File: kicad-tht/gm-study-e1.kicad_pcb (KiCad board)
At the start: 2 copper layers, 100 x 70 mm, 99 parts, among them J1 Conn_01x16, SW0 SW_SPDT, SW1 SW_SPDT, SW2 SW_SPDT, SW3 SW_SPDT, SW4 SW_SPDT, SW5 SW_SPDT, SW6 SW_SPDT, SW7 SW_SPDT, SW8 SW_SPDT, SW9 SW_SPDT, U1 SGM6603-5.0, U2 LSF0204, U3 LSF0204, U4 LSF0204

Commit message: file updates
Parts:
- removed JP1: Jumper, Connector_PinHeader_2.54mm:PinHeader_1x02_P2.54mm_Vertical
- R1, R10, R2, R3, R4, R5, R6, R7, R8, R9: value 10K -> 100K
- R11, R12, R13, R14, R15, R16, R17, R18, R19, R20: value 160 -> 200
- R30: value 160 -> 100
- RA1, RA10, RA11, RA12, RA2, RA3, RA4, RA5, RA6, RA7, RA8, RA9: value 180 -> 200
- moved BZ1 2.05 mm to (106.0, 73.0)
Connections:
- SW0 pad 3: Net-(JP1-Pad1) -> VIO_2V5
- SW1 pad 3: Net-(JP1-Pad1) -> VIO_2V5
- SW2 pad 3: Net-(JP1-Pad1) -> VIO_2V5
- SW3 pad 3: Net-(JP1-Pad1) -> VIO_2V5
- SW4 pad 3: Net-(JP1-Pad1) -> VIO_2V5
- SW5 pad 3: Net-(JP1-Pad1) -> VIO_2V5
- SW6 pad 3: Net-(JP1-Pad1) -> VIO_2V5
- SW7 pad 3: Net-(JP1-Pad1) -> VIO_2V5
- SW8 pad 3: Net-(JP1-Pad1) -> VIO_2V5
- SW9 pad 3: Net-(JP1-Pad1) -> VIO_2V5
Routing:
- net Net-(JP1-Pad1): track 64.2 -> 0.00 mm
- net VIO_2V5: track 180.7 -> 219.2 mm
- net IO_SA_A0: track 41.6 -> 39.6 mm
- net Net-(C6-Pad1): track 17.1 -> 17.6 mm
- net Net-(C4-Pad1): track 17.0 -> 17.5 mm
- net Net-(C3-Pad1): track 17.0 -> 17.5 mm
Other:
- board text removed: "SW0..9 pull-up"

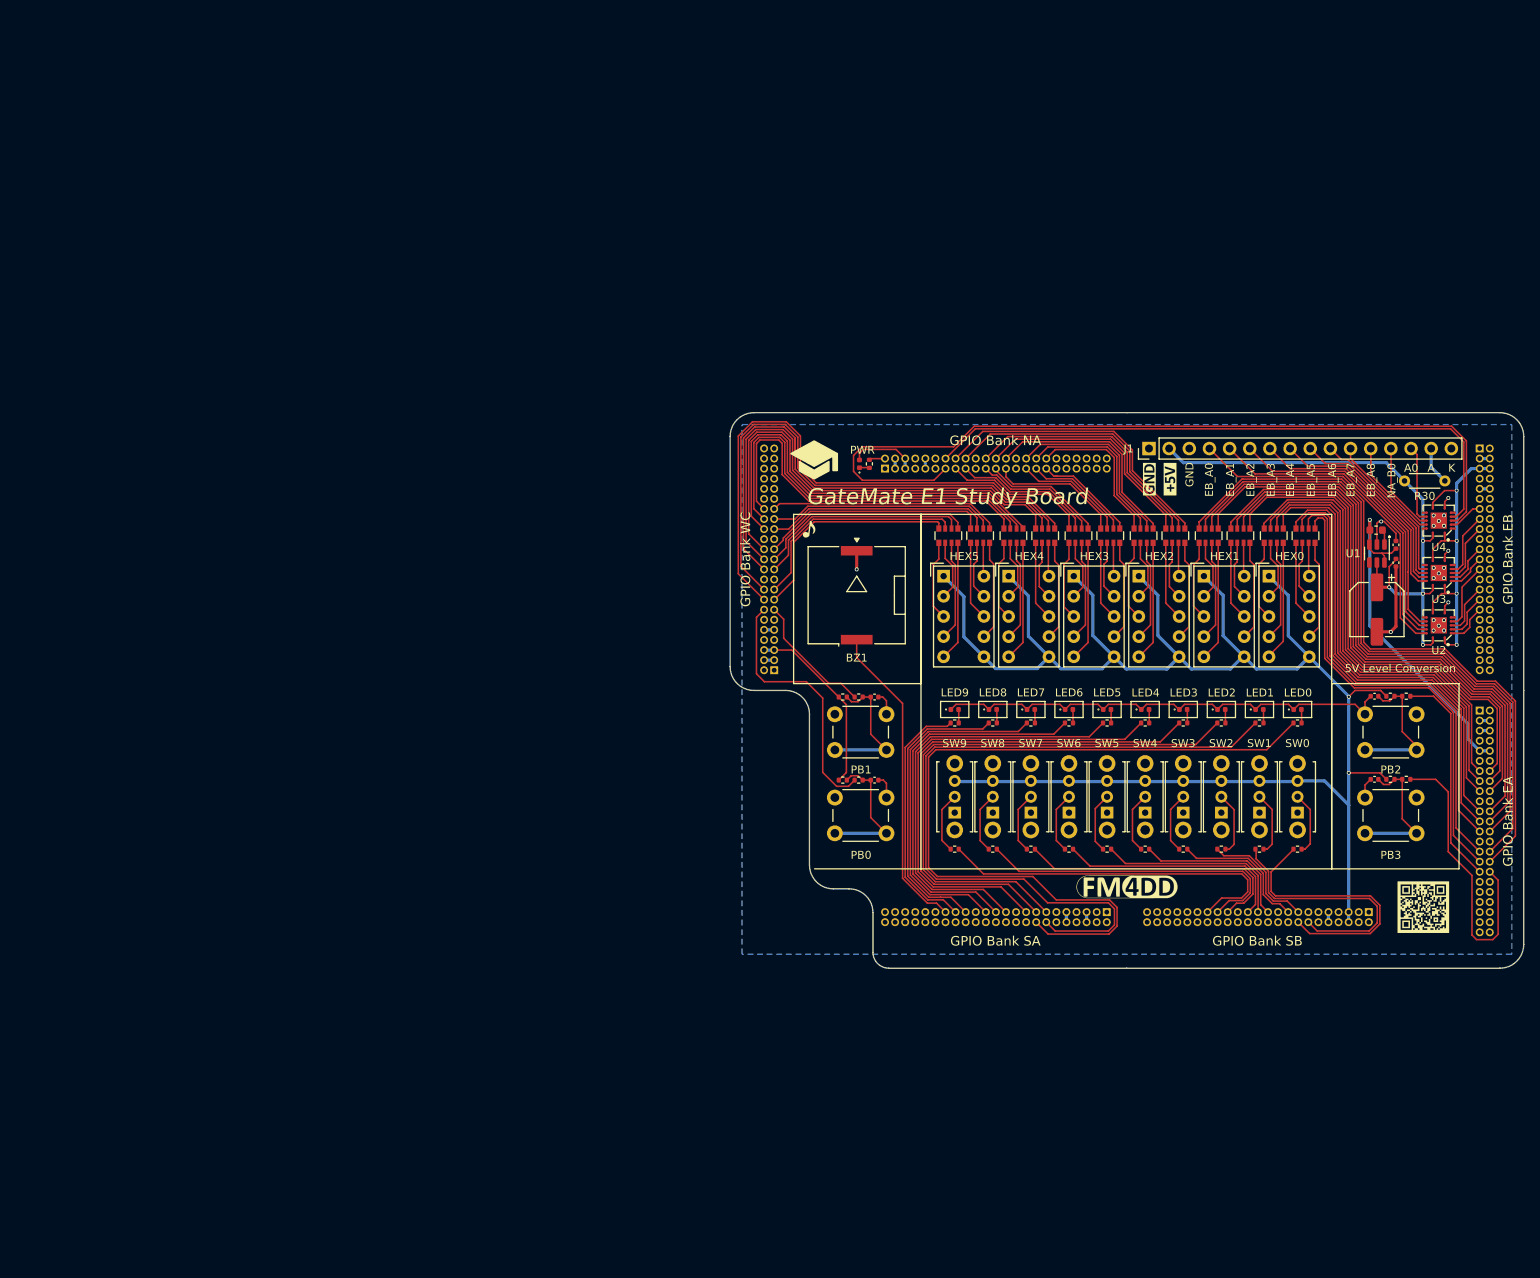
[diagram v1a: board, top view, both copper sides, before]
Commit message: New THT PCB v1.1 updates J1 level translation IC
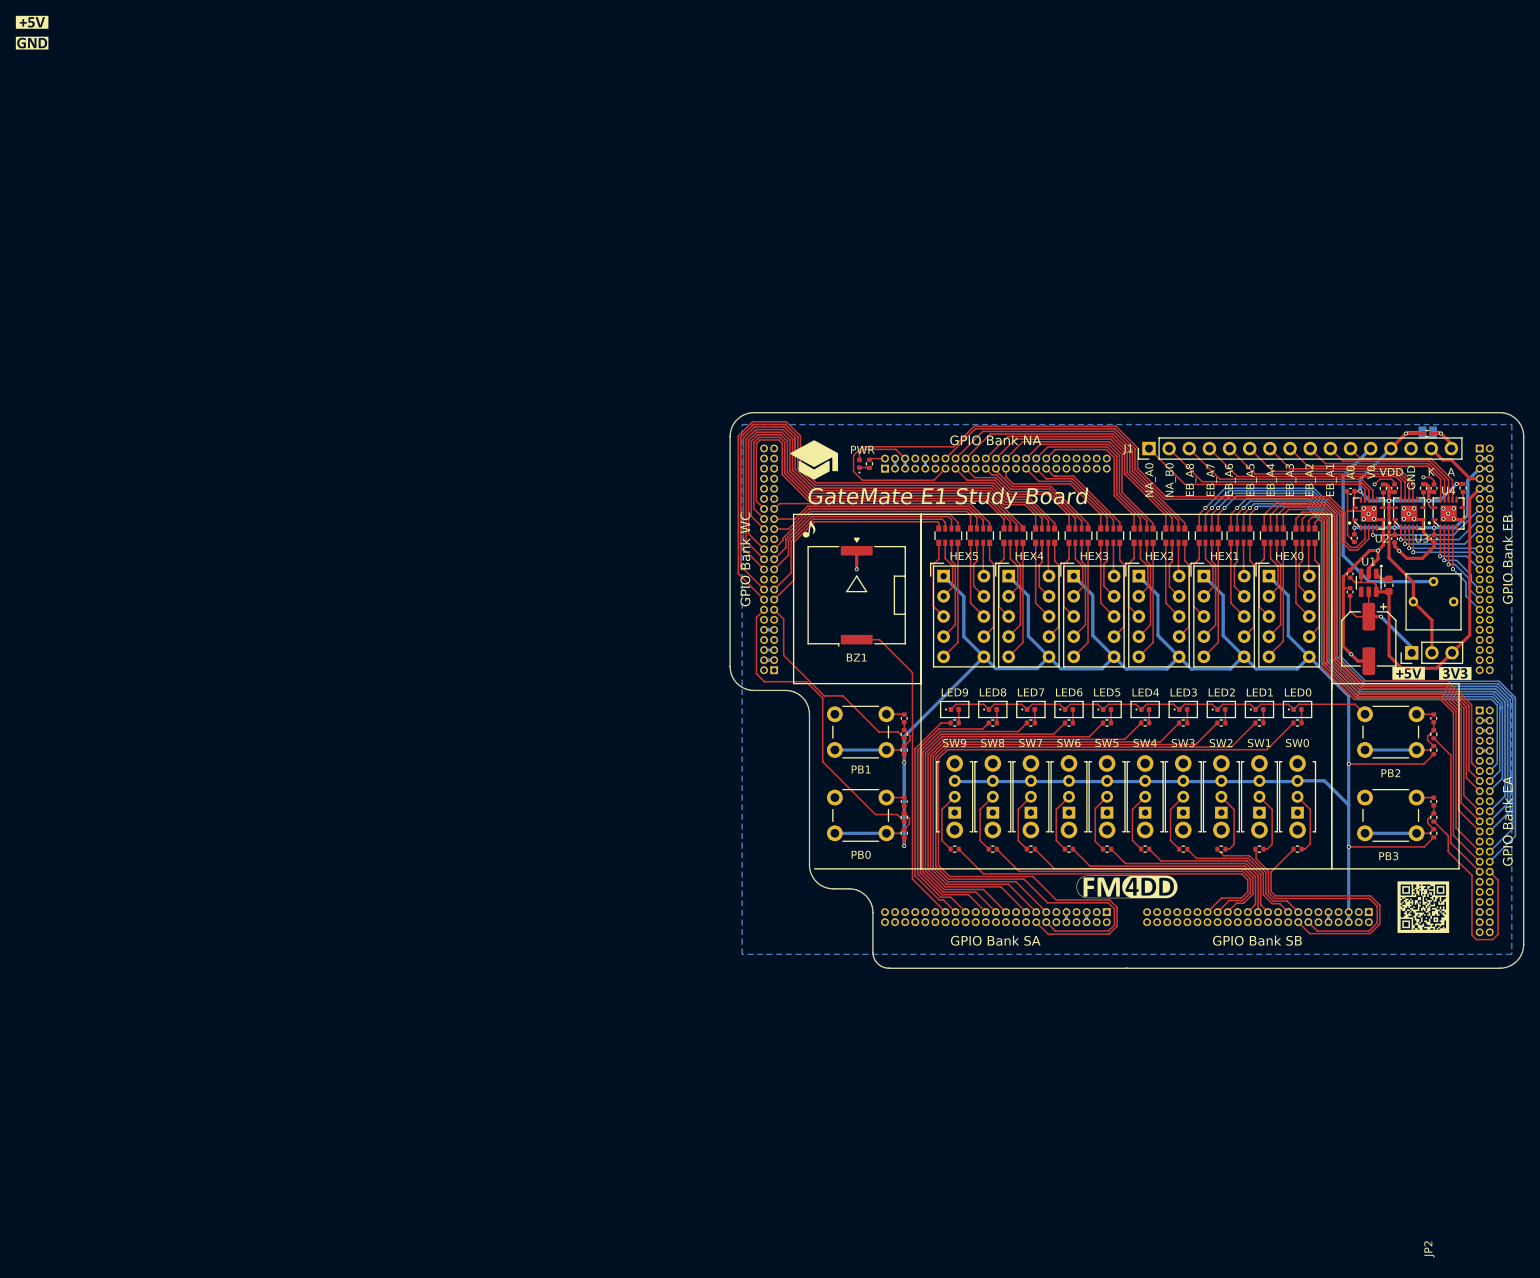
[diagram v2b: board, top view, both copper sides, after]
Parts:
- added C10: 0.1uF, Capacitor_SMD:C_0402_1005Metric, F.Cu at (178.7, 65.9)
- added C11: 0.1uF, Capacitor_SMD:C_0402_1005Metric, F.Cu at (173.7, 59.5)
- added C12: 0.1uF, Capacitor_SMD:C_0402_1005Metric, F.Cu at (168.2, 59.9)
- added C13: 0.1uF, Capacitor_SMD:C_0402_1005Metric, F.Cu at (178.7, 59.5)
- added C8: 0.1uF, Capacitor_SMD:C_0402_1005Metric, F.Cu at (168.7, 65.8)
- added C9: 0.1uF, Capacitor_SMD:C_0402_1005Metric, F.Cu at (173.7, 65.9)
- added JP1: SolderJumper_2_Open, Jumper:SolderJumper-2_P1.3mm_Open_Pad1.0x1.5mm, B.Cu at (177.9, 52.5)
- added JP2: UP_PWR, Connector_PinHeader_2.54mm:PinHeader_1x03_P2.54mm_Vertical, F.Cu at (175.9, 80.3)
- added LB5: Label_3V3, FM4DD:Label_3V3, F.Cu at (181.4, 82.9)
- added LB6: Label_5V, FM4DD:Label_5V, F.Cu at (175.5, 82.8)
- added R31: 10K, Resistor_SMD:R_0402_1005Metric, F.Cu at (172.3, 59.5)
- added R32: 10K, Resistor_SMD:R_0402_1005Metric, F.Cu at (177.4, 59.5)
- added R33: 10K, Resistor_SMD:R_0402_1005Metric, F.Cu at (182.4, 59.5)
- added RV1: 10K, FM4DD:Potentiometer_Bourns_3362P_Vertical, F.Cu at (178.6, 73.5)
- J1: value Conn_01x16 -> CharLCD_Header; footprint Connector_PinHeader_2.54mm:PinHeader_1x16_P2.54mm_Vertical -> FM4DD:CharLCD Header
- LED10: footprint FM4DD:LED_0402_FPGA -> FM4DD:LED_0402_no_frame
- R30: footprint Resistor_THT:R_Axial_DIN0204_L3.6mm_D1.6mm_P5.08mm_Horizontal -> Resistor_SMD:R_0402_1005Metric
- RA1, RA10, RA11, RA12, RA2, RA3, RA4, RA5, RA6, RA7, RA8, RA9: value 200 -> 180
- U2, U3, U4: value LSF0204 -> TXB104
- moved LB2 154.5 mm to (2.05, 0.81), turned to 0 degrees
- moved LB3 151.1 mm to (2.05, 3.43), turned to 0 degrees
- moved U2 16.6 mm to (170.5, 62.7), turned to 0 degrees
- moved R21 10.2 mm to (111.9, 103.0), turned to -90 degrees
- moved R22 10.2 mm to (111.9, 92.5), turned to -90 degrees
- moved R24 8.73 mm to (178.7, 103.0), turned to -90 degrees
- moved R23 8.72 mm to (178.7, 92.5), turned to -90 degrees
- moved U3 8.37 mm to (175.6, 62.7), turned to 0 degrees
- moved C6 7.98 mm to (178.7, 99.0), turned to 90 degrees
- moved C5 7.96 mm to (178.7, 88.5), turned to 90 degrees
- moved R25 7.42 mm to (111.9, 101.0), turned to -90 degrees
- moved R26 7.41 mm to (111.9, 90.5), turned to -90 degrees
- moved L1 7.13 mm to (173.0, 71.8), turned to 90 degrees
- moved C2 6.86 mm to (168.1, 72.6), turned to -90 degrees
- moved C1 6.83 mm to (168.1, 70.3)
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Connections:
- J1 pad 13: /data-out/NA_A0 -> /data-out/NA_B0
- J1 pad 14: /data-out/NA_B0 -> /data-out/NA_A0
- J1 pad 2: +5V -> /data-out/VDD
- J1 pad 3: GND -> /data-out/V0
- R21 pad 2: WC_VIO_2V5 -> VIO_2V5
- R22 pad 2: WC_VIO_2V5 -> VIO_2V5
- R30 pad 2: +5V -> /data-out/VDD
- U2 pad 10: /data-out/EB_A3 -> /data-out/EB_A8
- U2 pad 11: /data-out/EB_A2 -> /data-out/NA_B0
- U2 pad 12: /data-out/EB_A1 -> /data-out/NA_A0
- U2 pad 13: /data-out/EB_A0 -> unconnected-(U2-B1-Pad13)
- U2 pad 14: +5V -> /data-out/VDD
- U2 pad 2: IO_EB_A0 -> unconnected-(U2-A1-Pad2)
- U2 pad 3: IO_EB_A1 -> IO_NA_A0
- U2 pad 4: IO_EB_A2 -> IO_NA_B0
- U2 pad 5: IO_EB_A3 -> IO_EB_A8
- U2 pad 8: EB_VIO_IN -> Net-(U2-EN)
- U3 pad 10: /data-out/EB_A7 -> /data-out/EB_A4
- U3 pad 11: /data-out/EB_A6 -> /data-out/EB_A5
- U3 pad 12: /data-out/EB_A5 -> /data-out/EB_A6
- U3 pad 13: /data-out/EB_A4 -> /data-out/EB_A7
- U3 pad 14: +5V -> /data-out/VDD
- U3 pad 2: IO_EB_A4 -> IO_EB_A7
- U3 pad 3: IO_EB_A5 -> IO_EB_A6
- U3 pad 4: IO_EB_A6 -> IO_EB_A5
- U3 pad 5: IO_EB_A7 -> IO_EB_A4
- U3 pad 8: EB_VIO_IN -> Net-(U3-EN)
- U4 pad 10: /data-out/NA_B0 -> /data-out/EB_A0
- U4 pad 11: /data-out/NA_A0 -> /data-out/EB_A1
- U4 pad 12: /data-out/EB_A8 -> /data-out/EB_A2
- U4 pad 13: unconnected-(U4-Pad13) -> /data-out/EB_A3
- U4 pad 14: +5V -> /data-out/VDD
- U4 pad 2: unconnected-(U4-Pad2) -> IO_EB_A3
- U4 pad 3: IO_EB_A8 -> IO_EB_A2
- U4 pad 4: IO_NA_A0 -> IO_EB_A1
- U4 pad 5: IO_NA_B0 -> IO_EB_A0
- U4 pad 8: EB_VIO_IN -> Net-(U4-EN)
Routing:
- net /data-out/VDD: track 0.00 -> 62.3 mm, vias 0 -> 5
- net +5V: track 71.5 -> 15.3 mm, vias 4 -> 1
- net VIO_2V5: track 219.2 -> 261.3 mm, vias 2 -> 4
- net GND: track 93.9 -> 134.0 mm
- net /data-out/V0: track 0.00 -> 27.7 mm
- net /data-out/EB_A0: track 42.9 -> 16.9 mm
- net WC_VIO_2V5: track 23.1 -> 1.27 mm
- net /data-out/EB_A1: track 40.0 -> 18.9 mm
- net /data-out/NA_A0: track 11.1 -> 30.6 mm
- net /data-out/NA_B0: track 9.59 -> 28.5 mm
- net /data-out/EB_A2: track 37.1 -> 21.0 mm
- net /data-out/EB_A8: track 12.7 -> 26.4 mm
- net EB_VIO_IN: track 42.0 -> 28.4 mm, vias 4 -> 3
- net IO_NA_A0: track 105.2 -> 92.4 mm
- net IO_EB_A8: track 4.14 -> 15.7 mm, vias 0 -> 1
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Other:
- outline, holes or cut-outs redrawn
- board text added: "CharLCD_Header"
- board text added: "J1"
- board text added: "NA_A0"
- board text added: "RA1"
- board text added: "V0"
- board text added: "VDD"
- board text removed: "5V Level Conversion"
- board text removed: "EB_A0"
